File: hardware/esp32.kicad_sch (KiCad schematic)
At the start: 36 parts

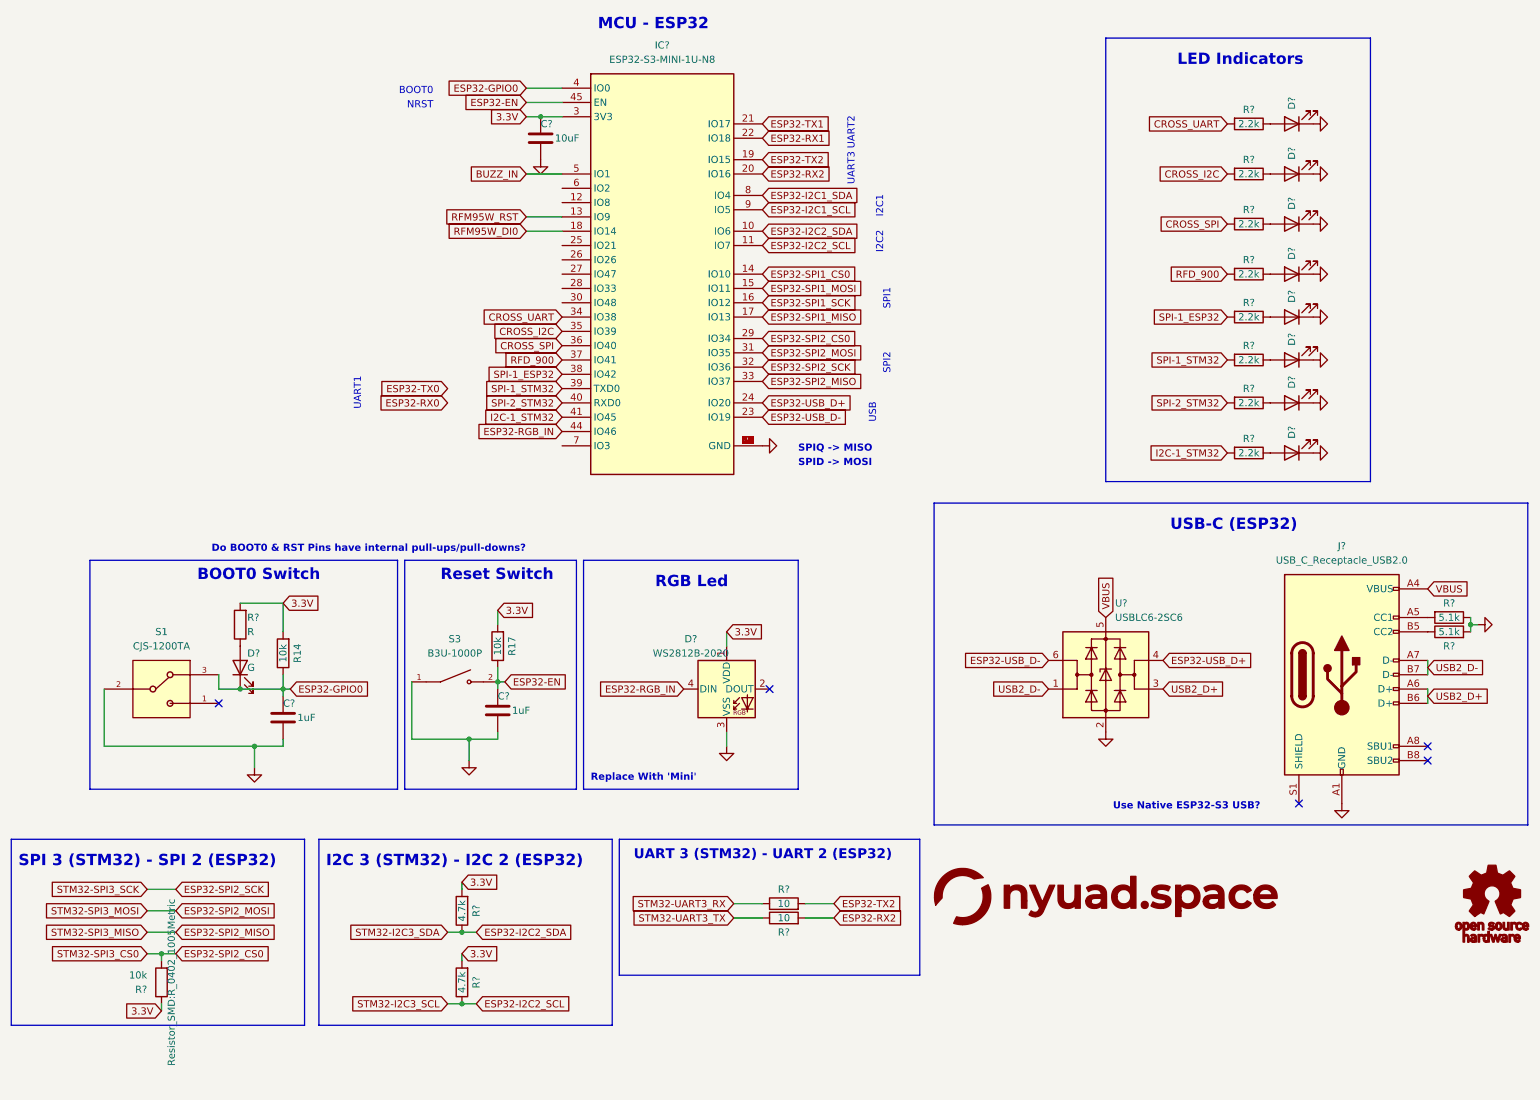
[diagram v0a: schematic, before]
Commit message: added BNO086
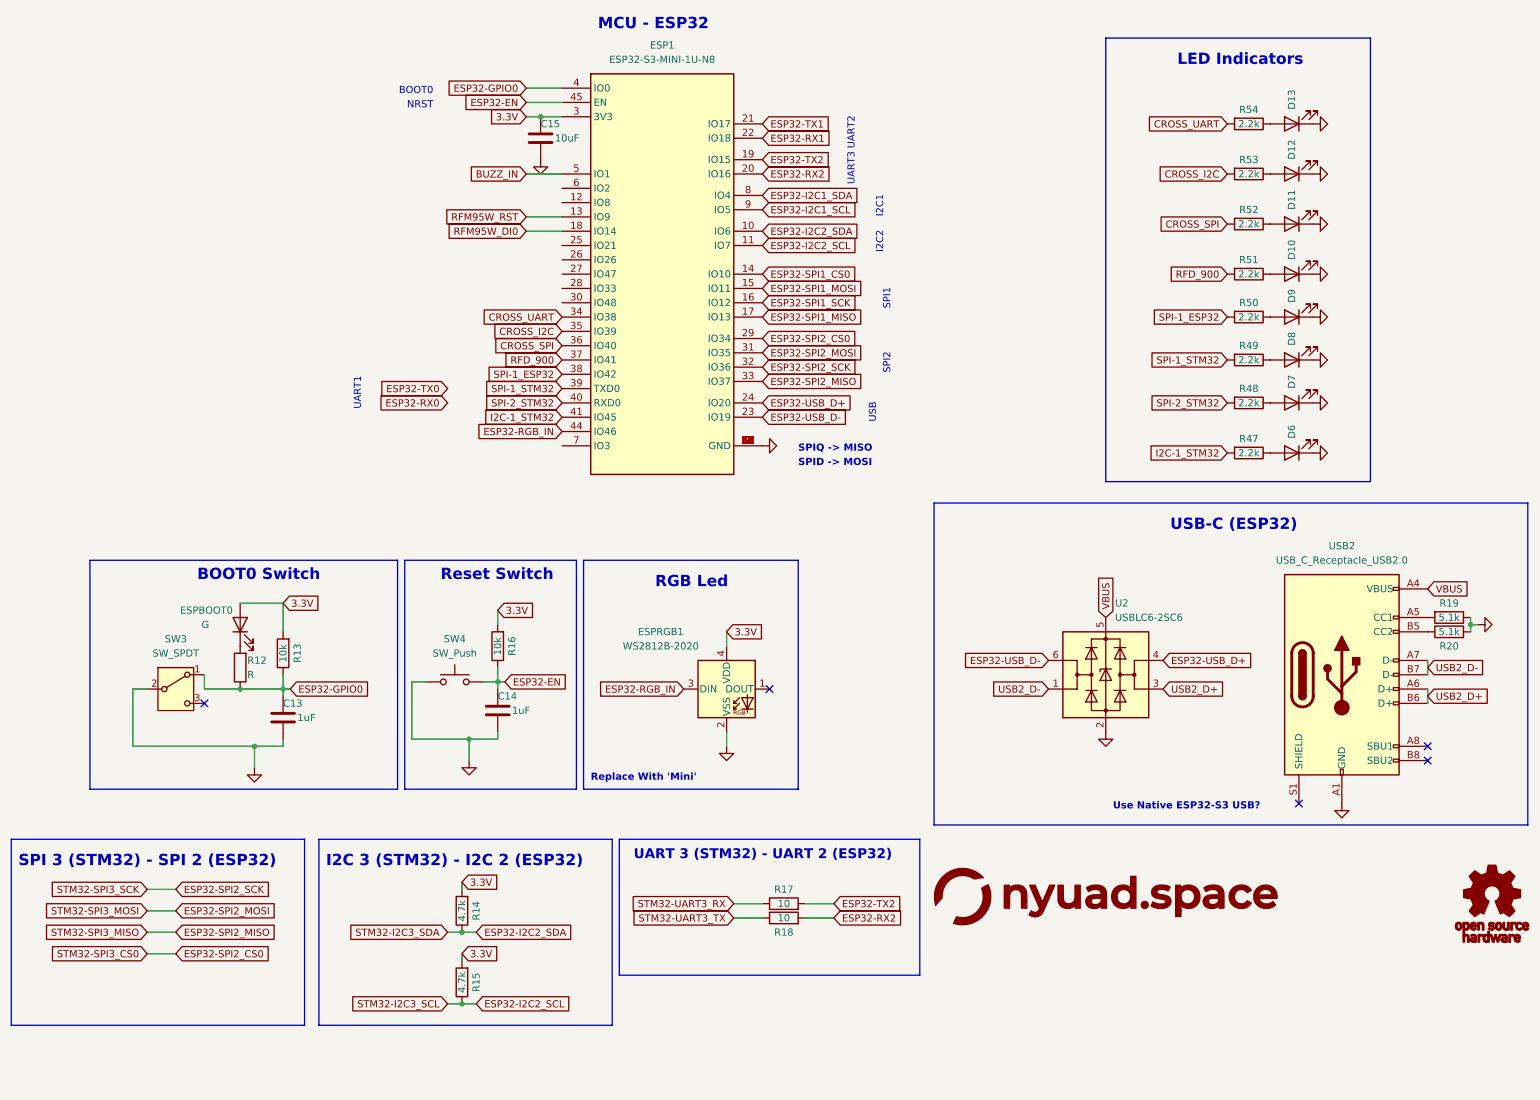
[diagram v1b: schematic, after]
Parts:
- removed D?: WS2812B-2020, LED_SMD:LED_WS2812B-2020_PLCC4_2.0x2.0mm, symbol LED:WS2812B
- removed R?: R, Resistor_SMD:R_0603_1608Metric, symbol Device:R
- removed R?: 10k, Resistor_SMD:R_0402_1005Metric, symbol Device:R
- removed S1: CJS-1200TA, CJS-1200TA:SW_CJS-1200TA, symbol CJS-1200TA:CJS-1200TA
- removed S3: B3U-1000P, B3U-1000P:SW_B3U-1000P, symbol B3U-1000P:B3U-1000P
- added ESPRGB1: WS2812B-2020, symbol LED:WS2812B-2020
- added R12: R, symbol Device:R
- added SW3: SW_SPDT, symbol Switch:SW_SPDT
- added SW4: SW_Push, symbol Switch:SW_Push
- C13, C14: renamed from C?; footprint Capacitor_SMD:C_0603_1608Metric -> (none)
- D10, D11, D12, D13, D6, D7, D8, D9: renamed from D?; footprint LED_SMD:LED_0402_1005Metric -> (none)
- ESP1: renamed from IC?; footprint ESP32S3MINI1UN8:ESP32S3MINI1UN8 -> (none)
- ESPBOOT0: renamed from D?; footprint LED_SMD:LED_0603_1608Metric -> (none)
- R13: renamed from R14; footprint Resistor_SMD:R_0603_1608Metric -> (none)
- R14, R15, R17, R18, R47, R48, R49, R50, R51, R52, R53, R54: renamed from R?; footprint Resistor_SMD:R_0402_1005Metric -> (none)
- R16: renamed from R17; footprint Resistor_SMD:R_0603_1608Metric -> (none)
- R19, R20: renamed from R?; footprint Resistor_SMD:R_0603_1608Metric -> (none)
- U2: renamed from U?; footprint Package_TO_SOT_SMD:SOT-23-6 -> (none)
- USB2: renamed from J?; footprint Connector_USB:USB_C_Receptacle_GCT_USB4105-xx-A_16P_TopMnt_Horizontal -> (none)
- gave numbers to parts that had none: 1
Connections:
- net 3.3V: now also ESPBOOT0.2 (A), ESPRGB1.4 (VDD)
- net ESP32-EN: now also SW4.2
- net ESP32-GPIO0: now also R12.1, SW3.1 (A); no longer ESPBOOT0.1 (K)
- net ESP32-RGB_IN: now also ESPRGB1.3 (DIN)
- net GND: now also ESPRGB1.2 (VSS), SW3.2 (B), SW4.1
- new net: ESPBOOT0.1 (K), R12.2
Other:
- note removed: "Do BOOT0 & RST Pins have internal pull-ups/pull-downs?"
- moved on the sheet: ESPBOOT0

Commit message: rev2 component placement
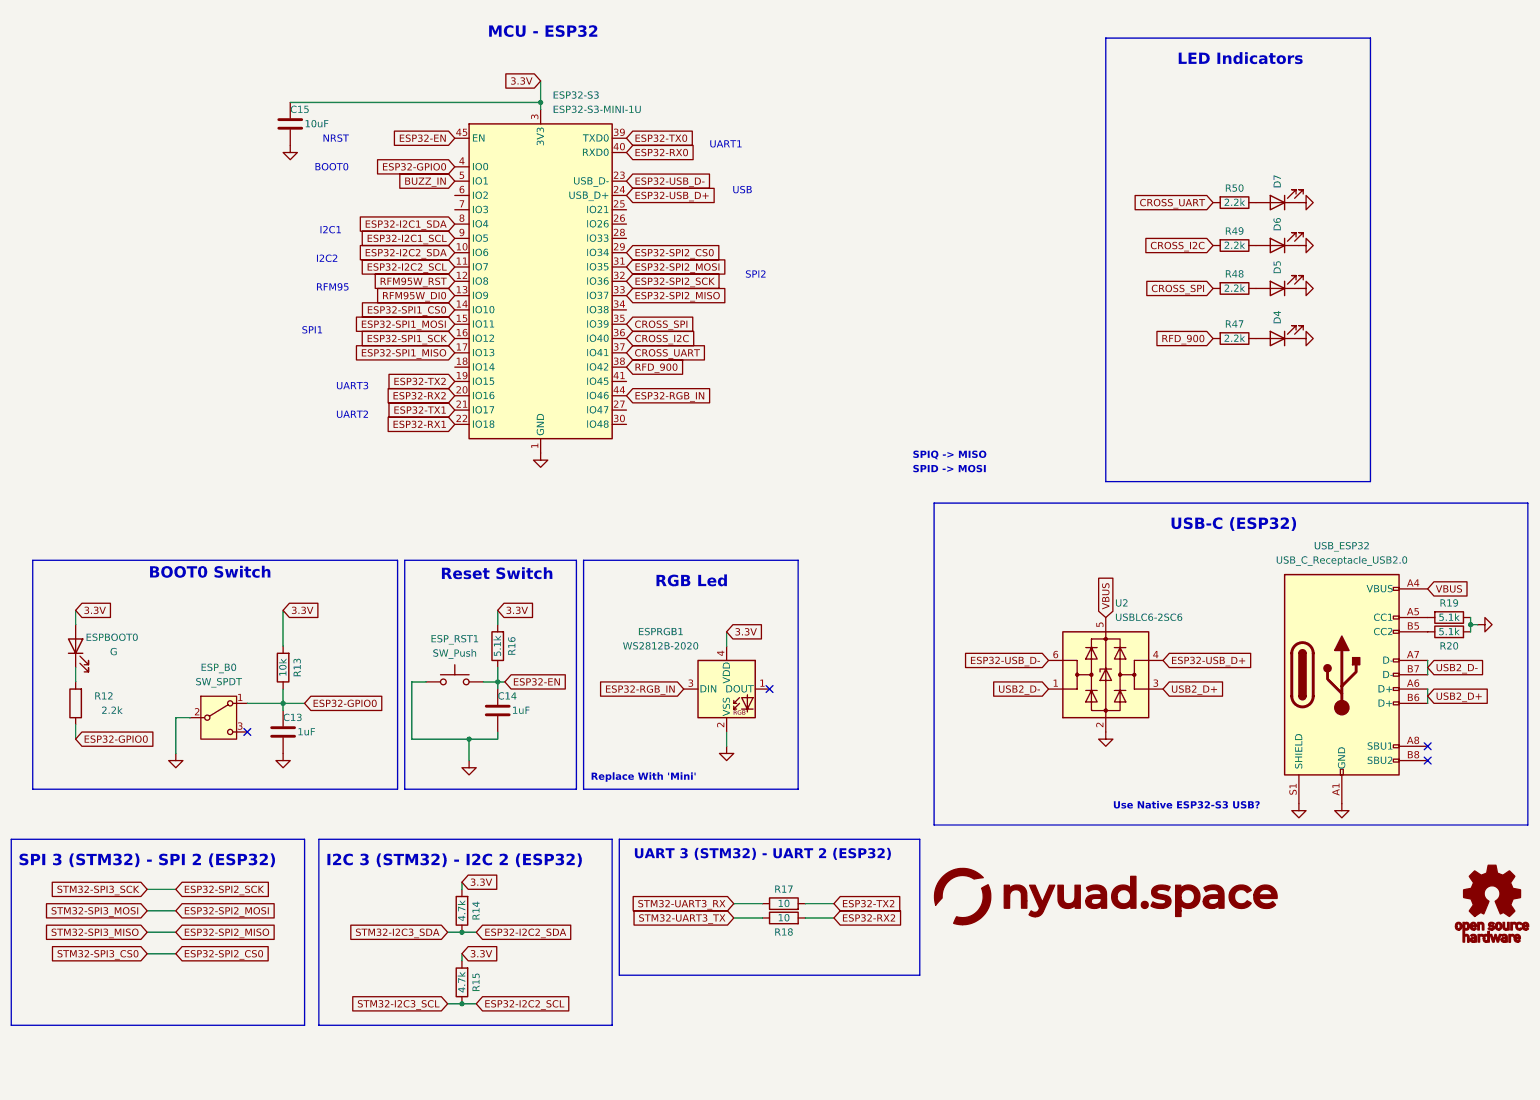
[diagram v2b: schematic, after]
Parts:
- removed D10, D11, D12, D13: LED, symbol Device:LED
- removed ESP1: ESP32-S3-MINI-1U-N8, symbol ESP32-S3-MINI-1U-N8:ESP32-S3-MINI-1U-N8
- removed R51, R52, R53, R54: 2.2k, symbol Device:R
- added ESP32-S3: ESP32-S3-MINI-1U, RF_Module:ESP32-S2-MINI-1U, symbol RF_Module:ESP32-S3-MINI-1U
- C13, C14: footprint (none) -> Capacitor_SMD:C_0603_1608Metric
- D4: renamed from D6; footprint (none) -> LED_SMD:LED_0603_1608Metric
- D5: renamed from D7; footprint (none) -> LED_SMD:LED_0603_1608Metric
- D6: renamed from D8; footprint (none) -> LED_SMD:LED_0603_1608Metric
- D7: renamed from D9; footprint (none) -> LED_SMD:LED_0603_1608Metric
- ESPBOOT0: footprint (none) -> LED_SMD:LED_0603_1608Metric
- ESPRGB1: footprint (none) -> LED_SMD:LED_WS2812B-2020_PLCC4_2.0x2.0mm
- ESP_B0: renamed from SW3; footprint (none) -> Button_Switch_SMD:SW_SPDT_PCM12
- ESP_RST1: renamed from SW4; footprint (none) -> Button_Switch_SMD:SW_SPST_B3U-1000P
- R12: value R -> 2.2k; footprint (none) -> Resistor_SMD:R_0603_1608Metric
- R13, R14, R15, R17, R18, R19, R20: footprint (none) -> Resistor_SMD:R_0402_1005Metric
- R16: value 10k -> 5.1k; footprint (none) -> Resistor_SMD:R_0402_1005Metric
- R47, R48, R49, R50: footprint (none) -> Resistor_SMD:R_0603_1608Metric
- U2: footprint (none) -> Package_TO_SOT_SMD:SOT-23-6
- USB_ESP32: renamed from USB2; footprint (none) -> Connector_USB:USB_C_Receptacle_G-Switch_GT-USB-7010ASV
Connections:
- net I2C-1_STM32 is gone; now on net RFD_900: R47.2
- net SPI-1_ESP32 is gone; now on net CROSS_UART: R50.2
- net SPI-1_STM32 is gone; now on net CROSS_I2C: R49.2
- net SPI-2_STM32 is gone; now on net CROSS_SPI: R48.2
- net 3.3V: now also ESP32-S3.3 (3V3)
- net BUZZ_IN: now also ESP32-S3.5 (IO1)
- net CROSS_I2C: now also ESP32-S3.36 (IO40)
- net CROSS_SPI: now also ESP32-S3.35 (IO39)
- net CROSS_UART: now also ESP32-S3.37 (IO41)
- net ESP32-EN: now also ESP32-S3.45 (EN)
- net ESP32-GPIO0: now also ESP32-S3.4 (IO0)
- net ESP32-I2C1_SCL: now also ESP32-S3.9 (IO5)
- net ESP32-I2C1_SDA: now also ESP32-S3.8 (IO4)
- net ESP32-I2C2_SCL: now also ESP32-S3.11 (IO7)
- net ESP32-I2C2_SDA: now also ESP32-S3.10 (IO6)
- net ESP32-RGB_IN: now also ESP32-S3.44 (IO46)
- net ESP32-RX0: now also ESP32-S3.40 (RXD0)
- net ESP32-RX1: now also ESP32-S3.22 (IO18)
- net ESP32-RX2: now also ESP32-S3.20 (IO16)
- net ESP32-SPI1_CS0: now also ESP32-S3.14 (IO10)
- net ESP32-SPI1_MISO: now also ESP32-S3.17 (IO13)
- net ESP32-SPI1_MOSI: now also ESP32-S3.15 (IO11)
- net ESP32-SPI1_SCK: now also ESP32-S3.16 (IO12)
- net ESP32-SPI2_CS0: now also ESP32-S3.29 (IO34)
- net ESP32-SPI2_MISO: now also ESP32-S3.33 (IO37)
- net ESP32-SPI2_MOSI: now also ESP32-S3.31 (IO35)
- net ESP32-SPI2_SCK: now also ESP32-S3.32 (IO36)
- net ESP32-TX0: now also ESP32-S3.39 (TXD0)
- net ESP32-TX1: now also ESP32-S3.21 (IO17)
- net ESP32-TX2: now also ESP32-S3.19 (IO15)
- net ESP32-USB_D+: now also ESP32-S3.24 (USB_D+)
- net ESP32-USB_D-: now also ESP32-S3.23 (USB_D-)
- net GND: now also USB_ESP32.S1 (SHIELD), ESP32-S3.1 (GND), ESP32-S3.2 (GND), ESP32-S3.42 (GND), ESP32-S3.43 (GND), ESP32-S3.46 (GND), ESP32-S3.47 (GND), ESP32-S3.48 (GND), ESP32-S3.49 (GND), ESP32-S3.50 (GND), ESP32-S3.51 (GND), ESP32-S3.52 (GND), ESP32-S3.53 (GND), ESP32-S3.54 (GND), ESP32-S3.55 (GND), ESP32-S3.56 (GND), ESP32-S3.57 (GND), ESP32-S3.58 (GND), ESP32-S3.59 (GND), ESP32-S3.60 (GND), ESP32-S3.61 (GND), ESP32-S3.62 (GND), ESP32-S3.63 (GND), ESP32-S3.64 (GND), ESP32-S3.65 (GND)
- net RFD_900: now also ESP32-S3.38 (IO42)
- net RFM95W_DI0: now also ESP32-S3.13 (IO9)
- net RFM95W_RST: now also ESP32-S3.12 (IO8)
- no-connect marks 5 -> 4
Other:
- note added: "RFM95"
- moved on the sheet: C13, C15, D4, D5, D6, D7, ESP_B0, R13, R47, R48, R49, R50
